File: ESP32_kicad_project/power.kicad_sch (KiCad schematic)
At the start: 25 parts, among them J2 USB_C_Receptacle_USB2.0_16P, J3 Screw_Terminal_01x02, Q1 AO3401A, U1 TPS56339DDC

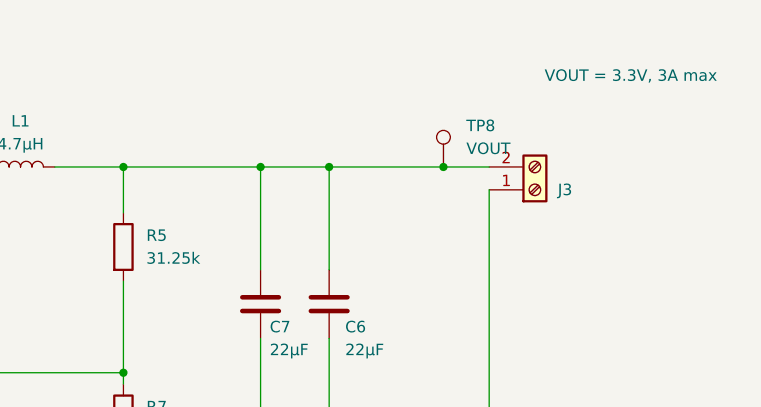
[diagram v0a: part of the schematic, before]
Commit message: created : esp32_core sheet, linked power between the power sheet and the esp32 core sheet
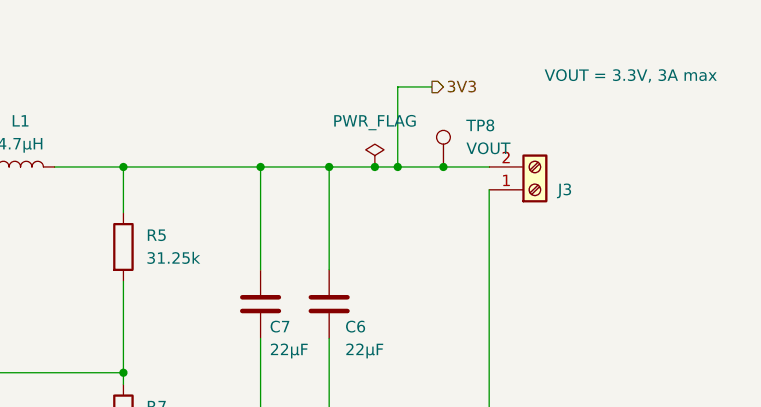
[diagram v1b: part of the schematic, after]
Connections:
- net 3V3: now reaches C6.1, C7.1, J3.2 (Pin_2), L1.2, R5.1, TP8.1
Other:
- title: (none) -> ESP32 Dev Board – Power Supply

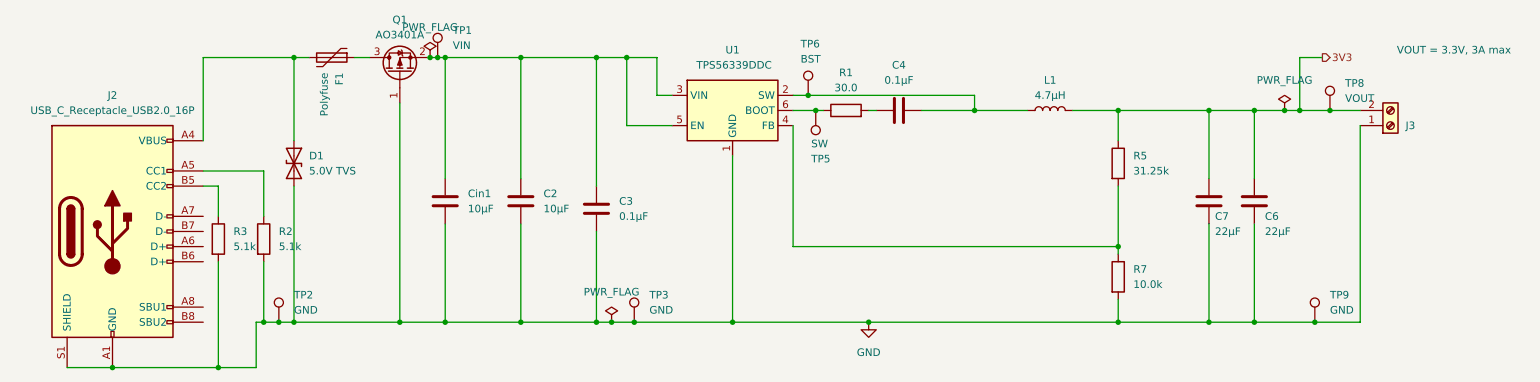
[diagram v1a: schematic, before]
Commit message: optimized everything with hierarchical labels, completed esp core, assigned footprints everywhere
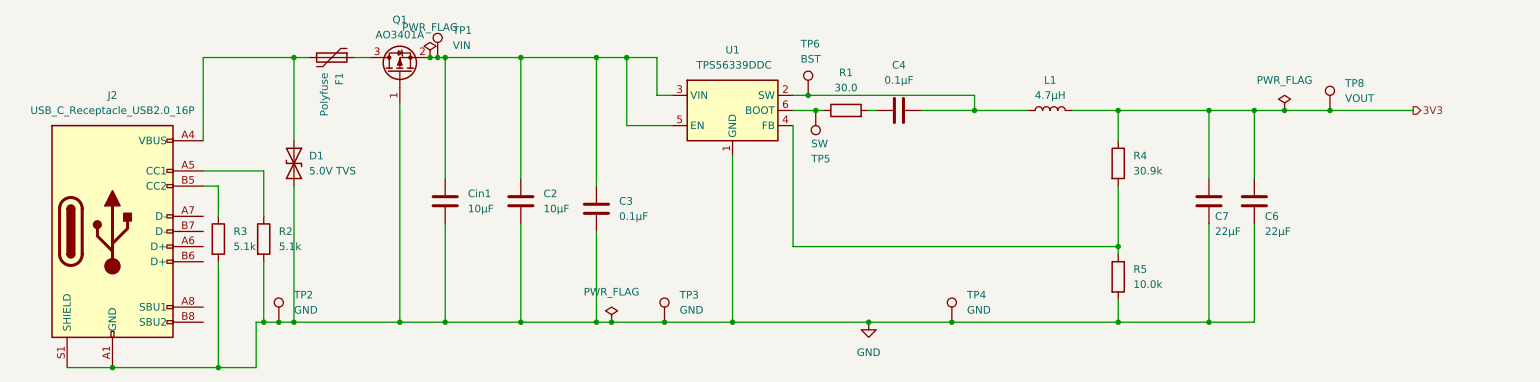
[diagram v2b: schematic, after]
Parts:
- removed J3: Screw_Terminal_01x02, symbol Connector:Screw_Terminal_01x02
- removed TP9: GND, TestPoint:TestPoint_Pad_D1.5mm, symbol Connector:TestPoint
- added TP4: GND, TestPoint:TestPoint_Pad_D1.5mm, symbol Connector:TestPoint
- R2, R3: footprint (none) -> Resistor_SMD:R_0603_1608Metric
- R4: renamed from R5; value 31.25k -> 30.9k
- renumbered R7 to R5
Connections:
- net GND: now also TP4.1
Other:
- moved on the sheet: TP3
